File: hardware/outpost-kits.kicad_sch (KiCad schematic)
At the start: 0 parts

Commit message: done dice v1, started vu meter
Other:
- added sheet dice (dice.kicad_sch)
- added sheet vu (vu.kicad_sch)
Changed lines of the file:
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@@
 	(generator_version "10.0")
 	(paper "A4")
+	(sheet
+		(at 113.665 29.845)
+		(size 51.435 34.29)
+		(exclude_from_sim no)
+		(in_bom yes)
+		(on_board yes)
+		(dnp no)
+		(fields_autoplaced yes)
+		(stroke
+			(width 0.1524)
+			(type solid)
+		)
+		(fill
+			(color 0 0 0 0)
+		)
+		(property "Sheetname" "vu"
+			(at 113.665 29.1334 0)
+			(show_name no)
+			(do_not_autoplace no)
+			(effects
+				(font
+					(size 1.27 1.27)
+				)
+				(justify left bottom)
+			)
+		)
+		(property "Sheetfile" "vu.kicad_sch"
+			(at 113.665 64.7196 0)
+			(show_name no)
+			(do_not_autoplace no)
+			(effects
+				(font
+					(size 1.27 1.27)
+				)
+				(justify left top)
+			)
+		)
+		(instances
+			(project "outpost-kits"
+				(path "/2b4acb03-95a4-4f7d-960f-b2e1be1f20ba"
+					(page "3")
+				)
+			)
+		)
+	)
+	(sheet
+		(at 30.48 29.845)
+		(size 48.26 34.29)
+		(exclude_from_sim no)
+		(in_bom yes)
+		(on_board yes)
+		(dnp no)
+		(fields_autoplaced yes)
+		(stroke
+			(width 0.1524)
+			(type solid)
+		)
+		(fill
+			(color 0 0 0 0)
+		)
+		(property "Sheetname" "dice"
+			(at 30.48 29.1334 0)
+			(show_name no)
+			(do_not_autoplace no)
+			(effects
+				(font
+					(size 1.27 1.27)
+				)
+				(justify left bottom)
+			)
+		)
+		(property "Sheetfile" "dice.kicad_sch"
+			(at 30.48 64.7196 0)
+			(show_name no)
+			(do_not_autoplace no)
+			(effects
+				(font
+					(size 1.27 1.27)
+				)
+				(justify left top)
+			)
+		)
+		(instances
+			(project "outpost-kits"
+				(path "/2b4acb03-95a4-4f7d-960f-b2e1be1f20ba"
+					(page "2")
+				)
+			)
+		)
+	)
 	(sheet_instances
 		(path "/"

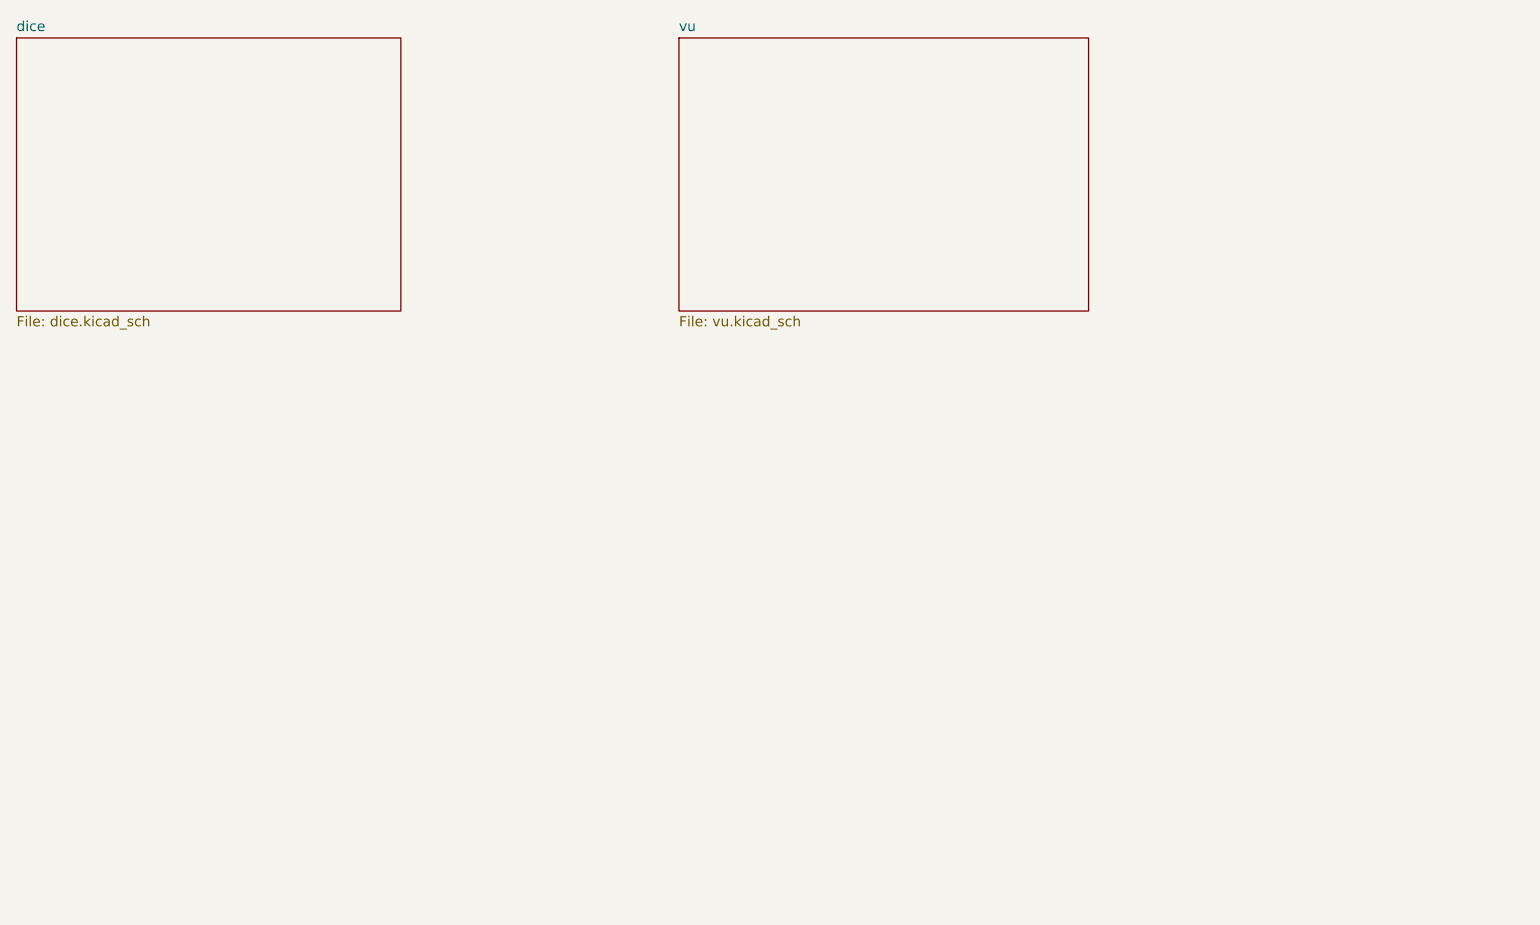
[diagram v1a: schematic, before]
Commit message: done first 3 pcbs
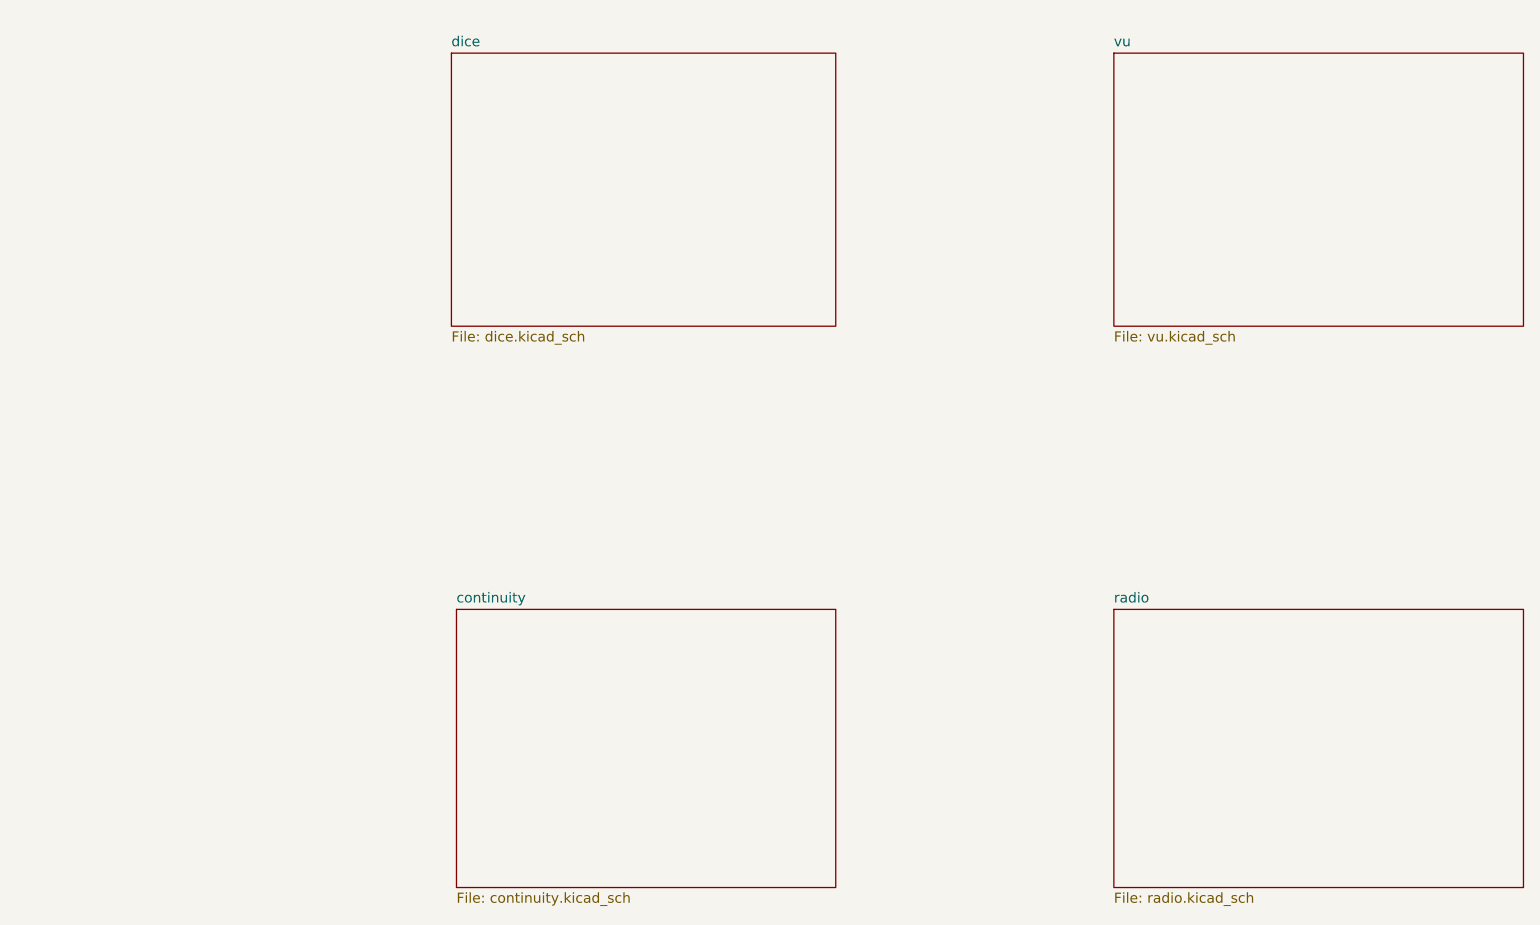
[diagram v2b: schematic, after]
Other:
- added sheet continuity (continuity.kicad_sch)
- added sheet radio (radio.kicad_sch)
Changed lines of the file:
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@@
 	(paper "A4")
 	(sheet
-		(at 113.665 29.845)
+		(at 168.275 31.75)
 		(size 51.435 34.29)
 		(exclude_from_sim no)
@@
 		)
 		(property "Sheetname" "vu"
-			(at 113.665 29.1334 0)
+			(at 168.275 31.0384 0)
 			(show_name no)
 			(do_not_autoplace no)
@@
 		)
 		(property "Sheetfile" "vu.kicad_sch"
-			(at 113.665 64.7196 0)
+			(at 168.275 66.6246 0)
 			(show_name no)
 			(do_not_autoplace no)
@@
 	)
 	(sheet
-		(at 30.48 29.845)
+		(at 168.275 101.6)
+		(size 51.435 34.925)
+		(exclude_from_sim no)
+		(in_bom yes)
+		(on_board yes)
+		(dnp no)
+		(fields_autoplaced yes)
+		(stroke
+			(width 0.1524)
+			(type solid)
+		)
+		(fill
+			(color 0 0 0 0)
+		)
+		(property "Sheetname" "radio"
+			(at 168.275 100.8884 0)
+			(show_name no)
+			(do_not_autoplace no)
+			(effects
+				(font
+					(size 1.27 1.27)
+				)
+				(justify left bottom)
+			)
+		)
+		(property "Sheetfile" "radio.kicad_sch"
+			(at 168.275 137.1096 0)
+			(show_name no)
+			(do_not_autoplace no)
+			(effects
+				(font
+					(size 1.27 1.27)
+				)
+				(justify left top)
+			)
+		)
+		(instances
+			(project "outpost-kits"
+				(path "/2b4acb03-95a4-4f7d-960f-b2e1be1f20ba"
+					(page "5")
+				)
+			)
+		)
+	)
+	(sheet
+		(at 85.725 101.6)
+		(size 47.625 34.925)
+		(exclude_from_sim no)
+		(in_bom yes)
+		(on_board yes)
+		(dnp no)
+		(fields_autoplaced yes)
+		(stroke
+			(width 0.1524)
+			(type solid)
+		)
+		(fill
+			(color 0 0 0 0)
+		)
+		(property "Sheetname" "continuity"
+			(at 85.725 100.8884 0)
+			(show_name no)
+			(do_not_autoplace no)
+			(effects
+				(font
+					(size 1.27 1.27)
+				)
+				(justify left bottom)
+			)
+		)
+		(property "Sheetfile" "continuity.kicad_sch"
+			(at 85.725 137.1096 0)
+			(show_name no)
+			(do_not_autoplace no)
+			(effects
+				(font
+					(size 1.27 1.27)
+				)
+				(justify left top)
+			)
+		)
+		(instances
+			(project "outpost-kits"
+				(path "/2b4acb03-95a4-4f7d-960f-b2e1be1f20ba"
+					(page "4")
+				)
+			)
+		)
+	)
+	(sheet
+		(at 85.09 31.75)
 		(size 48.26 34.29)
 		(exclude_from_sim no)
@@
 		)
 		(property "Sheetname" "dice"
-			(at 30.48 29.1334 0)
+			(at 85.09 31.0384 0)
 			(show_name no)
 			(do_not_autoplace no)
@@
 		)
 		(property "Sheetfile" "dice.kicad_sch"
-			(at 30.48 64.7196 0)
+			(at 85.09 66.6246 0)
 			(show_name no)
 			(do_not_autoplace no)

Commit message: done v1?
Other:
- sheet radio renamed conductivity
- sheet conductivity: file radio.kicad_sch -> conductivity.kicad_sch
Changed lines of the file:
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@@
 			(color 0 0 0 0)
 		)
-		(property "Sheetname" "radio"
+		(property "Sheetname" "conductivity"
 			(at 168.275 100.8884 0)
 			(show_name no)
@@
 			)
 		)
-		(property "Sheetfile" "radio.kicad_sch"
+		(property "Sheetfile" "conductivity.kicad_sch"
 			(at 168.275 137.1096 0)
 			(show_name no)
